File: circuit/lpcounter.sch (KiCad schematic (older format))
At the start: 25 parts, among them IC1 ATTINY85V-P, M1 SYN115, P1 CONN_01X08, P2 CONN_02X01, P3 Hole_3.5mm, P4 Hole_3.5mm, P5 Hole_3.5mm, P6 Hole_3.5mm, P7 BAT+, P8 BAT-

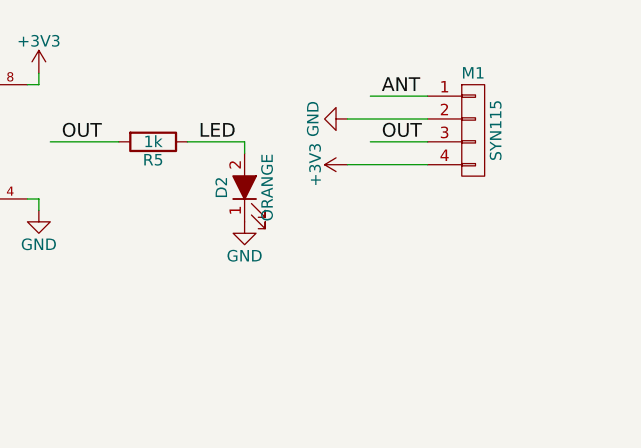
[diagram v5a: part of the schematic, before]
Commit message: placeholder for both SMD and TH LED
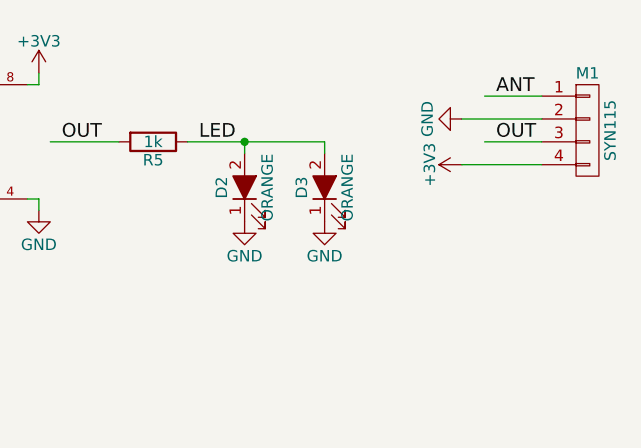
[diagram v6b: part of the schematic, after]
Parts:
- added D3: ORANGE, LEDs:LED_1206, symbol LED_ALT
- D2: footprint Diodes_SMD:MiniMELF_Handsoldering -> LEDs:LED-5MM
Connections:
- wire segments 31 -> 32
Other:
- moved on the sheet: M1
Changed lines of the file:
@@
 IN0
 $Comp
-L GND #PWR28
+L GND #PWR01
 U 1 1 591028B9
 P 7900 3850
-F 0 "#PWR28" H 7900 3600 50  0001 C CNN
+F 0 "#PWR01" H 7900 3600 50  0001 C CNN
 F 1 "GND" H 7900 3700 50  0000 C CNN
 F 2 "" H 7900 3850 50  0000 C CNN
@@
 RESETn
 $Comp
-L +3V3 #PWR27
+L +3V3 #PWR02
 U 1 1 59102AB8
 P 7900 3250
-F 0 "#PWR27" H 7900 3100 50  0001 C CNN
+F 0 "#PWR02" H 7900 3100 50  0001 C CNN
 F 1 "+3V3" H 7900 3390 50  0000 C CNN
 F 2 "" H 7900 3250 50  0000 C CNN
@@
 $EndComp
 $Comp
-L +3V3 #PWR21
+L +3V3 #PWR03
 U 1 1 59102B87
 P 6200 5000
-F 0 "#PWR21" H 6200 4850 50  0001 C CNN
+F 0 "#PWR03" H 6200 4850 50  0001 C CNN
 F 1 "+3V3" H 6200 5140 50  0000 C CNN
 F 2 "" H 6200 5000 50  0000 C CNN
@@
 $EndComp
 $Comp
-L GND #PWR22
+L GND #PWR04
 U 1 1 59102F4B
 P 6200 5300
-F 0 "#PWR22" H 6200 5050 50  0001 C CNN
+F 0 "#PWR04" H 6200 5050 50  0001 C CNN
 F 1 "GND" H 6200 5150 50  0000 C CNN
 F 2 "" H 6200 5300 50  0000 C CNN
@@
 L CONN_01X04 M1
 U 1 1 591033D1
-P 9800 3500
-F 0 "M1" H 9800 3750 50  0000 C CNN
-F 1 "SYN115" V 9900 3500 50  0000 C CNN
-F 2 "syn115:SYN115" H 9800 3500 50  0001 C CNN
-F 3 "" H 9800 3500 50  0000 C CNN
-	1    9800 3500
-	1    0    0    -1
-$EndComp
-Wire Wire Line
-	9600 3350 9350 3350
-Text Label 9400 3350 0    60   ~ 0
+P 10300 3500
+F 0 "M1" H 10300 3750 50  0000 C CNN
+F 1 "SYN115" V 10400 3500 50  0000 C CNN
+F 2 "syn115:SYN115" H 10300 3500 50  0001 C CNN
+F 3 "" H 10300 3500 50  0000 C CNN
+	1    10300 3500
+	1    0    0    -1
+$EndComp
+Wire Wire Line
+	10100 3350 9850 3350
+Text Label 9900 3350 0    60   ~ 0
 ANT
 $Comp
-L GND #PWR30
+L GND #PWR05
 U 1 1 591034EC
-P 9250 3450
-F 0 "#PWR30" H 9250 3200 50  0001 C CNN
-F 1 "GND" H 9250 3300 50  0000 C CNN
-F 2 "" H 9250 3450 50  0000 C CNN
-F 3 "" H 9250 3450 50  0000 C CNN
-	1    9250 3450
+P 9750 3450
+F 0 "#PWR05" H 9750 3200 50  0001 C CNN
+F 1 "GND" H 9750 3300 50  0000 C CNN
+F 2 "" H 9750 3450 50  0000 C CNN
+F 3 "" H 9750 3450 50  0000 C CNN
+	1    9750 3450
 	0    1    1    0
 $EndComp
 $Comp
-L +3V3 #PWR31
+L +3V3 #PWR06
 U 1 1 59103508
-P 9250 3650
-F 0 "#PWR31" H 9250 3500 50  0001 C CNN
-F 1 "+3V3" H 9250 3790 50  0000 C CNN
-F 2 "" H 9250 3650 50  0000 C CNN
-F 3 "" H 9250 3650 50  0000 C CNN
-	1    9250 3650
-	0    -1   -1   0
-$EndComp
-Wire Wire Line
-	9250 3450 9600 3450
-Wire Wire Line
-	9250 3650 9600 3650
-Wire Wire Line
-	9600 3550 9350 3550
-Text Label 9400 3550 0    60   ~ 0
+P 9750 3650
+F 0 "#PWR06" H 9750 3500 50  0001 C CNN
+F 1 "+3V3" H 9750 3790 50  0000 C CNN
+F 2 "" H 9750 3650 50  0000 C CNN
+F 3 "" H 9750 3650 50  0000 C CNN
+	1    9750 3650
+	0    -1   -1   0
+$EndComp
+Wire Wire Line
+	9750 3450 10100 3450
+Wire Wire Line
+	9750 3650 10100 3650
+Wire Wire Line
+	10100 3550 9850 3550
+Text Label 9900 3550 0    60   ~ 0
 OUT
 $Comp
@@
 	1550 3850 2000 3850
 $Comp
-L GND #PWR2
+L GND #PWR07
 U 1 1 59103D18
 P 1550 3350
-F 0 "#PWR2" H 1550 3100 50  0001 C CNN
+F 0 "#PWR07" H 1550 3100 50  0001 C CNN
 F 1 "GND" H 1550 3200 50  0000 C CNN
 F 2 "" H 1550 3350 50  0000 C CNN
@@
 $EndComp
 $Comp
-L GND #PWR3
+L GND #PWR08
 U 1 1 59103D4F
 P 1550 3550
-F 0 "#PWR3" H 1550 3300 50  0001 C CNN
+F 0 "#PWR08" H 1550 3300 50  0001 C CNN
 F 1 "GND" H 1550 3400 50  0000 C CNN
 F 2 "" H 1550 3550 50  0000 C CNN
@@
 $EndComp
 $Comp
-L GND #PWR4
+L GND #PWR09
 U 1 1 59103D6D
 P 1550 3750
-F 0 "#PWR4" H 1550 3500 50  0001 C CNN
+F 0 "#PWR09" H 1550 3500 50  0001 C CNN
 F 1 "GND" H 1550 3600 50  0000 C CNN
 F 2 "" H 1550 3750 50  0000 C CNN
@@
 $EndComp
 $Comp
-L GND #PWR5
+L GND #PWR010
 U 1 1 59103DA4
 P 1550 3950
-F 0 "#PWR5" H 1550 3700 50  0001 C CNN
+F 0 "#PWR010" H 1550 3700 50  0001 C CNN
 F 1 "GND" H 1550 3800 50  0000 C CNN
 F 2 "" H 1550 3950 50  0000 C CNN
@@
 IN0
 $Comp
-L GND #PWR9
+L GND #PWR011
 U 1 1 5910458F
 P 2550 3900
-F 0 "#PWR9" H 2550 3650 50  0001 C CNN
+F 0 "#PWR011" H 2550 3650 50  0001 C CNN
 F 1 "GND" H 2550 3750 50  0000 C CNN
 F 2 "" H 2550 3900 50  0000 C CNN
@@
 $EndComp
 $Comp
-L +3V3 #PWR8
+L +3V3 #PWR012
 U 1 1 591045FE
 P 2550 3200
-F 0 "#PWR8" H 2550 3050 50  0001 C CNN
+F 0 "#PWR012" H 2550 3050 50  0001 C CNN
 F 1 "+3V3" H 2550 3340 50  0000 C CNN
 F 2 "" H 2550 3200 50  0000 C CNN
@@
 $EndComp
 $Comp
-L +3V3 #PWR23
+L +3V3 #PWR013
 U 1 1 5910481E
 P 6700 5000
-F 0 "#PWR23" H 6700 4850 50  0001 C CNN
+F 0 "#PWR013" H 6700 4850 50  0001 C CNN
 F 1 "+3V3" H 6700 5140 50  0000 C CNN
 F 2 "" H 6700 5000 50  0000 C CNN
@@
 $EndComp
 $Comp
-L GND #PWR24
+L GND #PWR014
 U 1 1 59104863
 P 6700 5300
-F 0 "#PWR24" H 6700 5050 50  0001 C CNN
+F 0 "#PWR014" H 6700 5050 50  0001 C CNN
 F 1 "GND" H 6700 5150 50  0000 C CNN
 F 2 "" H 6700 5300 50  0000 C CNN
@@
 IN1
 $Comp
-L GND #PWR12
+L GND #PWR015
 U 1 1 59104EB6
 P 3150 3900
-F 0 "#PWR12" H 3150 3650 50  0001 C CNN
+F 0 "#PWR015" H 3150 3650 50  0001 C CNN
 F 1 "GND" H 3150 3750 50  0000 C CNN
 F 2 "" H 3150 3900 50  0000 C CNN
@@
 $EndComp
 $Comp
-L +3V3 #PWR11
+L +3V3 #PWR016
 U 1 1 59104EBC
 P 3150 3200
-F 0 "#PWR11" H 3150 3050 50  0001 C CNN
+F 0 "#PWR016" H 3150 3050 50  0001 C CNN
 F 1 "+3V3" H 3150 3340 50  0000 C CNN
 F 2 "" H 3150 3200 50  0000 C CNN
@@
 IN2
 $Comp
-L GND #PWR14
+L GND #PWR017
 U 1 1 5910502C
 P 3750 3900
-F 0 "#PWR14" H 3750 3650 50  0001 C CNN
+F 0 "#PWR017" H 3750 3650 50  0001 C CNN
 F 1 "GND" H 3750 3750 50  0000 C CNN
 F 2 "" H 3750 3900 50  0000 C CNN
@@
 $EndComp
 $Comp
-L +3V3 #PWR13
+L +3V3 #PWR018
 U 1 1 59105032
 P 3750 3200
-F 0 "#PWR13" H 3750 3050 50  0001 C CNN
+F 0 "#PWR018" H 3750 3050 50  0001 C CNN
 F 1 "+3V3" H 3750 3340 50  0000 C CNN
 F 2 "" H 3750 3200 50  0000 C CNN
@@
 IN3
 $Comp
-L GND #PWR16
+L GND #PWR019
 U 1 1 59105048
 P 4350 3900
-F 0 "#PWR16" H 4350 3650 50  0001 C CNN
+F 0 "#PWR019" H 4350 3650 50  0001 C CNN
 F 1 "GND" H 4350 3750 50  0000 C CNN
 F 2 "" H 4350 3900 50  0000 C CNN
@@
 $EndComp
 $Comp
-L +3V3 #PWR15
+L +3V3 #PWR020
 U 1 1 5910504E
 P 4350 3200
-F 0 "#PWR15" H 4350 3050 50  0001 C CNN
+F 0 "#PWR020" H 4350 3050 50  0001 C CNN
 F 1 "+3V3" H 4350 3340 50  0000 C CNN
 F 2 "" H 4350 3200 50  0000 C CNN
@@
 F 0 "D2" H 8800 3850 50  0000 C CNN
 F 1 "ORANGE" H 8800 3650 50  0000 C CNN
-F 2 "Diodes_SMD:MiniMELF_Handsoldering" H 8800 3750 50  0001 C CNN
+F 2 "LEDs:LED-5MM" H 8800 3750 50  0001 C CNN
 F 3 "" H 8800 3750 50  0000 C CNN
 	1    8800 3750
@@
 	8800 3600 8800 3550
 Wire Wire Line
-	8800 3550 8550 3550
+	8550 3550 9150 3550
 Text Label 8000 3550 0    60   ~ 0
 OUT
@@
 	8250 3550 7950 3550
 $Comp
-L GND #PWR29
+L GND #PWR021
 U 1 1 59106156
 P 8800 3900
-F 0 "#PWR29" H 8800 3650 50  0001 C CNN
+F 0 "#PWR021" H 8800 3650 50  0001 C CNN
 F 1 "GND" H 8800 3750 50  0000 C CNN
 F 2 "" H 8800 3900 50  0000 C CNN
@@
 $EndComp
 $Comp
-L +3V3 #PWR25
+L +3V3 #PWR022
 U 1 1 5910891F
 P 7250 5000
-F 0 "#PWR25" H 7250 4850 50  0001 C CNN
+F 0 "#PWR022" H 7250 4850 50  0001 C CNN
 F 1 "+3V3" H 7250 5140 50  0000 C CNN
 F 2 "" H 7250 5000 50  0000 C CNN
@@
 $EndComp
 $Comp
-L GND #PWR26
+L GND #PWR023
 U 1 1 59108925
 P 7250 5300
-F 0 "#PWR26" H 7250 5050 50  0001 C CNN
+F 0 "#PWR023" H 7250 5050 50  0001 C CNN
 F 1 "GND" H 7250 5150 50  0000 C CNN
 F 2 "" H 7250 5300 50  0000 C CNN
@@
 $EndComp
 $Comp
-L +3V3 #PWR17
+L +3V3 #PWR024
 U 1 1 591067BD
 P 4350 4500
-F 0 "#PWR17" H 4350 4350 50  0001 C CNN
+F 0 "#PWR024" H 4350 4350 50  0001 C CNN
 F 1 "+3V3" H 4350 4640 50  0000 C CNN
 F 2 "" H 4350 4500 50  0000 C CNN
@@
 Connection ~ 4350 4950
 $Comp
-L GND #PWR18
+L GND #PWR025
 U 1 1 59106977
 P 4350 5500
-F 0 "#PWR18" H 4350 5250 50  0001 C CNN
+F 0 "#PWR025" H 4350 5250 50  0001 C CNN
 F 1 "GND" H 4350 5350 50  0000 C CNN
 F 2 "" H 4350 5500 50  0000 C CNN
@@
 $EndComp
 $Comp
-L GND #PWR7
+L GND #PWR026
 U 1 1 59119C8B
 P 2250 4800
-F 0 "#PWR7" H 2250 4550 50  0001 C CNN
+F 0 "#PWR026" H 2250 4550 50  0001 C CNN
 F 1 "GND" H 2250 4650 50  0000 C CNN
 F 2 "" H 2250 4800 50  0000 C CNN
@@
 $EndComp
 $Comp
-L GND #PWR10
+L GND #PWR027
 U 1 1 59119D27
 P 2800 4800
-F 0 "#PWR10" H 2800 4550 50  0001 C CNN
+F 0 "#PWR027" H 2800 4550 50  0001 C CNN
 F 1 "GND" H 2800 4650 50  0000 C CNN
 F 2 "" H 2800 4800 50  0000 C CNN
@@
 $EndComp
 $Comp
-L GND #PWR1
+L GND #PWR028
 U 1 1 59119EC9
 P 1150 4800
-F 0 "#PWR1" H 1150 4550 50  0001 C CNN
+F 0 "#PWR028" H 1150 4550 50  0001 C CNN
 F 1 "GND" H 1150 4650 50  0000 C CNN
 F 2 "" H 1150 4800 50  0000 C CNN
@@
 $EndComp
 $Comp
-L GND #PWR6
+L GND #PWR029
 U 1 1 59119ED5
 P 1700 4800
-F 0 "#PWR6" H 1700 4550 50  0001 C CNN
+F 0 "#PWR029" H 1700 4550 50  0001 C CNN
 F 1 "GND" H 1700 4650 50  0000 C CNN
 F 2 "" H 1700 4800 50  0000 C CNN
@@
 $EndComp
 $Comp
-L +3V3 #PWR19
+L +3V3 #PWR030
 U 1 1 5911EF06
 P 5550 4800
-F 0 "#PWR19" H 5550 4650 50  0001 C CNN
+F 0 "#PWR030" H 5550 4650 50  0001 C CNN
 F 1 "+3V3" H 5550 4940 50  0000 C CNN
 F 2 "" H 5550 4800 50  0000 C CNN
@@
 $EndComp
 $Comp
-L GND #PWR20
+L GND #PWR031
 U 1 1 591217AB
 P 5550 5800
-F 0 "#PWR20" H 5550 5550 50  0001 C CNN
+F 0 "#PWR031" H 5550 5550 50  0001 C CNN
 F 1 "GND" H 5550 5650 50  0000 C CNN
 F 2 "" H 5550 5800 50  0000 C CNN
@@
 	1    0    0    -1
 $EndComp
+$Comp
+L LED_ALT D3
+U 1 1 5912D9C6
+P 9150 3750
+F 0 "D3" H 9150 3850 50  0000 C CNN
+F 1 "ORANGE" H 9150 3650 50  0000 C CNN
+F 2 "LEDs:LED_1206" H 9150 3750 50  0001 C CNN
+F 3 "" H 9150 3750 50  0000 C CNN
+	1    9150 3750
+	0    -1   -1   0
+$EndComp
+Wire Wire Line
+	9150 3550 9150 3600
+Connection ~ 8800 3550
+$Comp
+L GND #PWR032
+U 1 1 5912DAF3
+P 9150 3900
+F 0 "#PWR032" H 9150 3650 50  0001 C CNN
+F 1 "GND" H 9150 3750 50  0000 C CNN
+F 2 "" H 9150 3900 50  0000 C CNN
+F 3 "" H 9150 3900 50  0000 C CNN
+	1    9150 3900
+	1    0    0    -1
+$EndComp
